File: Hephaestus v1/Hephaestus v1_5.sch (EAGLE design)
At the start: 31 parts, among them IC1 NC7SZ14P5X

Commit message: Schematic for Hephaestus V1_5 is essentially complete, need to select C2 and C1 values
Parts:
- removed PU_CL, PU_DA: 5k, resistor:R-US_R2512
- removed R_DEAD: (no value), resistor:R-US_R2512
- added ACS1: ACS712, heph_custom_comp:ACS712
- added C10: (no value), eagle-ltspice:CC0603
- added C11, C12: 4.7 uF, eagle-ltspice:CC0603
- added C13: 1 nF, eagle-ltspice:CC0603
- added C14: 0.1 uF, eagle-ltspice:CC0603
- added C15, C16, C9: 400 nF, eagle-ltspice:CC0603
- added D5: 12V, diode:DIODE-DO-214AC
- added D6, D7, D8, D9: 1N4148, diode:DIODE-DO35-10
- added IC2: NC7SZ14P5X, 74xx-little-de:NC7SZ14P5X
- added R10, R11, R12, R9: 1000, resistor:R-US_R2512
- added R13, R5: 5000, resistor:R-US_R2512
- added R6, R8: 55000, resistor:R-US_R2512
- added R7: (no value), resistor:R-US_R2512
- added U$23, U$24, U$25, U$26: STD15NF10, heph_custom_comp:STD15NF10
- added U$28: MCP3021, heph_custom_comp:MCP3021
- added U$6: A4957, heph_custom_comp:A4957
- C3: value (none) -> 400 nF
- D1, D2, D3, D4: value (none) -> 1N4148
- R1, R2, R3, R4: value (none) -> 1000
- renumbered CBYP to C8
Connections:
- removed net N$7 (its old number): U$1.RESET
- new net CA_B: C15.2, U$6.CA
- new net CB_B: C16.2, U$6.CB
- new net CUR_SENSE_B: ACS1.IP_N1, ACS1.IP_N2, D6.C, D8.C, U$23.D, U$24.D
- new net GHA_B: R10.2, R2.2, U$24.G
- new net GHB_B: R12.2, U$23.G
- new net GLA_B: R9.2, U$25.G
- new net GLB_B: R11.2, U$26.G
- new net MCU_GPIO_B_INV: IC2G$1.O, U$6.ALO
- new net MCU_SPD_B: U$6.BHI
- new net MOTOR_B+: C15.1, D6.A, D7.C, U$24.S, U$25.D, U$6.SA
- new net MOTOR_B-: C16.1, D8.A, D9.C, U$23.S, U$26.D, U$6.SB
- new net N$23: ACS1.VIOUT, U$28.AIN
- new net N$24: ACS1.FILTER, C13.2
- new net N$25: IC2G$1.I
- new net N$26: R9.1, U$6.GLA
- new net N$27: R11.1, U$6.GLB
- new net N$28: R12.1, U$6.GHB
- new net N$29: C10.2, U$6.VREG
- new net N$30: C4.2, U$6.CP2
- new net N$31: C4.1, U$6.CP1
- new net N$6: D5.A, R7.1, SIHFR9010.G
- new net RDEAD: R5.2, U$1.RESET
- new net RDEAD1: R13.2, U$6.RESET
- net CA_S: now also C9.2, U$1.CA; no longer C3.1, U$1.SA
- net CB_S: now also C3.2, U$1.CB; no longer C4.1, U$1.SB
- net GHA_S: no longer R2.2
- net GND: now also ACS1.GND, C10.1, C11.1, C12.1, C13.1, C14.1, D7.A, D9.A, R13.1, R5.1, R6.1, R7.2, R8.1, SV1.4, U$25.S, U$26.S, U$28.GND, U$6.AGND, U$6.GND_1, U$6.GND_2, U$6.GND_3; no longer R_DEAD.1, SIHFR9010.G, SV1.7
- net I2C_SCL_S: now also SV1.6, U$28.SCL; no longer PU_CL.2, SV1.5
- net I2C_SDA_S: now also SV1.5, U$28.SDA; no longer PU_DA.2, SV1.6
- net MCU_DIR_B: now also U$6.BLO
- net MCU_DIR_S: now also SV1.7; no longer SV1.4
- net MCU_FAULT_B: now also U$6.FAULT
- net MCU_FAULT_S: now also SV1.10; no longer SV1.1
- net MCU_GPIO_B: now also U$6.AHI
- net MCU_GPIO_S: now also SV1.9; no longer SV1.2
- net MCU_PWM_S: now also SV1.8; no longer SV1.3
- net MOTOR_S+: now also C9.1, U$1.SA
- net MOTOR_S-: now also C3.1, U$1.SB
- net N$12: now also R8.2, U$6.TDEAD; no longer C3.2, U$1.CA
- net N$14: now also R10.1, U$6.GHA; no longer C4.2, U$1.CB
- net N$8: now also R6.2; no longer R_DEAD.2
- net PP12V_2: now also ACS1.IP_P1, ACS1.IP_P2, C11.2, D5.C, SV3.1, U$6.VBB; no longer SV3.3
- net PP3V3: now also SV1.3; no longer SV1.8
- net PP5V: now also ACS1.VCC, C12.2, C14.2, SV1.1, SV1.2, U$28.VCC, U$6.VDD; no longer PU_CL.1, PU_DA.1, SV1.10, SV1.9
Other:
- note added: "Braking Current Sensing"
- note added: "Braking H-Bridge"
- note added: "SMAZ12"
- moved on the sheet: C1, C2, C3, C4, D1, D2, D3, D4, IC1, R1, R2, R3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

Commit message: Small changes and updates to the catch-diodes and P/N
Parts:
- removed C10, C4: (no value), eagle-ltspice:CC0603
- removed C11, C12: 4.7 uF, eagle-ltspice:CC0603
- removed C15, C16: 400 nF, eagle-ltspice:CC0603
- removed D6, D7, D8, D9: 1N4148, diode:DIODE-DO35-10
- removed IC2: NC7SZ14P5X, 74xx-little-de:NC7SZ14P5X
- removed R12: 1000, resistor:R-US_R2512
- removed R13: 5000, resistor:R-US_R2512
- removed U$18, U$28: MCP3021, heph_custom_comp:MCP3021
- removed U$23, U$24, U$25, U$26: STD15NF10, heph_custom_comp:STD15NF10
- added IC3: NC7SZ14P5X, 74xx-little-de:NC7SZ14P5X
- added U$22: MCP6L01, heph_custom_comp:MCP6L01
- added U$35: MCP3246, heph_custom_comp:MCP3246
- C1: value (none) -> 470 nF
- C2: value (none) -> 20 uF
- C3, C9: value 400 nF -> 1 uF
- D1, D2, D3, D4: value 1N4148 -> PMEG6020ETR; device diode:DIODE-DO35-10 -> heph_custom_comp:PMEG6020ETR
- R1, R2, R3, R4: value 1000 -> 100
- R10, R11, R9: value 1000 -> 5k
- R5: value 5000 -> 33k
- R6, R8: value 55000 -> 5k
- R7: value (none) -> 10000
- SIHFR9010: value FDD4141TO252 -> ATP302; device transistor-fet:FDD4141TO252 -> heph_custom_comp:ATP302
- U$10, U$5, U$8, U$9: value STD15NF10 -> FDMS037N08B; device heph_custom_comp:STD15NF10 -> heph_custom_comp:FDMS037N08B
- U$6: value A4957 -> MCP6L01; device heph_custom_comp:A4957 -> heph_custom_comp:MCP6L01
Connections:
- net MCU_GPIO_S_INV renamed MCU_DIR_S_INV
- net N$6 renamed RVP_G
- removed net CA_B: C15.2, U$6.CA
- removed net CB_B: C16.2, U$6.CB
- removed net GHB_B: R12.2, U$23.G
- removed net GLA_B: R9.2, U$25.G
- removed net GLB_B: R11.2, U$26.G
- removed net I2C_SCL_S: SV1.6, U$18.SCL, U$28.SCL
- removed net I2C_SDA_S: SV1.5, U$18.SDA, U$28.SDA
- removed net MCU_GPIO_B_INV: IC2G$1.O, U$6.ALO
- removed net MCU_SPD_B: U$6.BHI
- removed net MCU_SPD_S: U$1.BHI
- removed net MOTOR_B+: C15.1, D6.A, D7.C, U$24.S, U$25.D, U$6.SA
- removed net MOTOR_B-: C16.1, D8.A, D9.C, U$23.S, U$26.D, U$6.SB
- removed net N$12: R8.2, U$6.TDEAD
- removed net N$14: R10.1, U$6.GHA
- removed net N$21: ACS712.VIOUT, U$18.AIN
- removed net N$23: ACS1.VIOUT, U$28.AIN
- removed net N$25: IC2G$1.I
- removed net N$26: R9.1, U$6.GLA
- removed net N$27: R11.1, U$6.GLB
- removed net N$28: R12.1, U$6.GHB
- removed net N$29: C10.2, U$6.VREG
- removed net N$30: C4.2, U$6.CP2
- removed net N$31: C4.1, U$6.CP1
- removed net N$5: IC1G$1.I
- removed net RDEAD: R5.2, U$1.RESET
- removed net RDEAD1: R13.2, U$6.RESET
- new net CS_1: ACS712.VIOUT, U$35.CH1+
- new net CS_2: ACS1.VIOUT, U$35.CH2+
- new net I2C_SCL: SV1.6, U$35.SCL
- new net I2C_SDA: SV1.5, U$35.SDA
- new net MCU_PWM_S_INV: IC3G$1.O, U$1.BHI
- new net N$32: R5.1, U$1.RESET
- net CUR_SENSE_B: no longer D6.C, D8.C, U$23.D, U$24.D
- net GHA_B: no longer R10.2, U$24.G
- net GND: now also IC1P.GND, IC3P.GND, U$35.CH1-, U$35.CH2-, U$35.VSS; no longer C10.1, C11.1, C12.1, D7.A, D9.A, R13.1, R5.1, R8.1, U$18.GND, U$25.S, U$26.S, U$28.GND, U$6.AGND, U$6.GND_1, U$6.GND_2, U$6.GND_3
- net MCU_DIR_B: now also SV2.4; no longer SV2.1, U$6.BLO
- net MCU_DIR_S: now also IC1G$1.I
- net MCU_FAULT_B: now also SV2.1; no longer SV2.4, U$6.FAULT
- net MCU_GPIO_B: now also SV2.2; no longer SV2.3, U$6.AHI
- net MCU_GPIO_S: no longer U$1.AHI
- net MCU_PWM_B: now also SV2.3; no longer SV2.2
- net MCU_PWM_S: now also IC3G$1.I, U$1.AHI
- net PP12V_2: no longer C11.2, U$6.VBB
- net PP5V: now also IC1P.VCC, IC3P.VCC, R5.2, U$35.VDD; no longer C12.2, U$18.VCC, U$28.VCC, U$6.VDD
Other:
- note added: "Board to Steering Motor Conn"
- note added: "Boards to Brakes Motor Conn"
- note added: "Braking Current Sensor"
- note added: "Steering / Braking ADC"
- note added: "Steering Curent Sensor"
- note added: "UPDATE BRAKING H-BRIDGE"
- note added: "for r6 between 3, 240 kOhms, tdead ~ 50 + 7200 / (1.2 + (200 / rdead))"
- note removed: "Board to Steering Motor"
- note removed: "Boards to Brakes Motor"
- note removed: "Braking Current Sensing"
- note removed: "Steering Current Sensing"
- moved on the sheet: C13, C14, C7, C8, IC1, R10, R11, R5, R8, R9, SV2

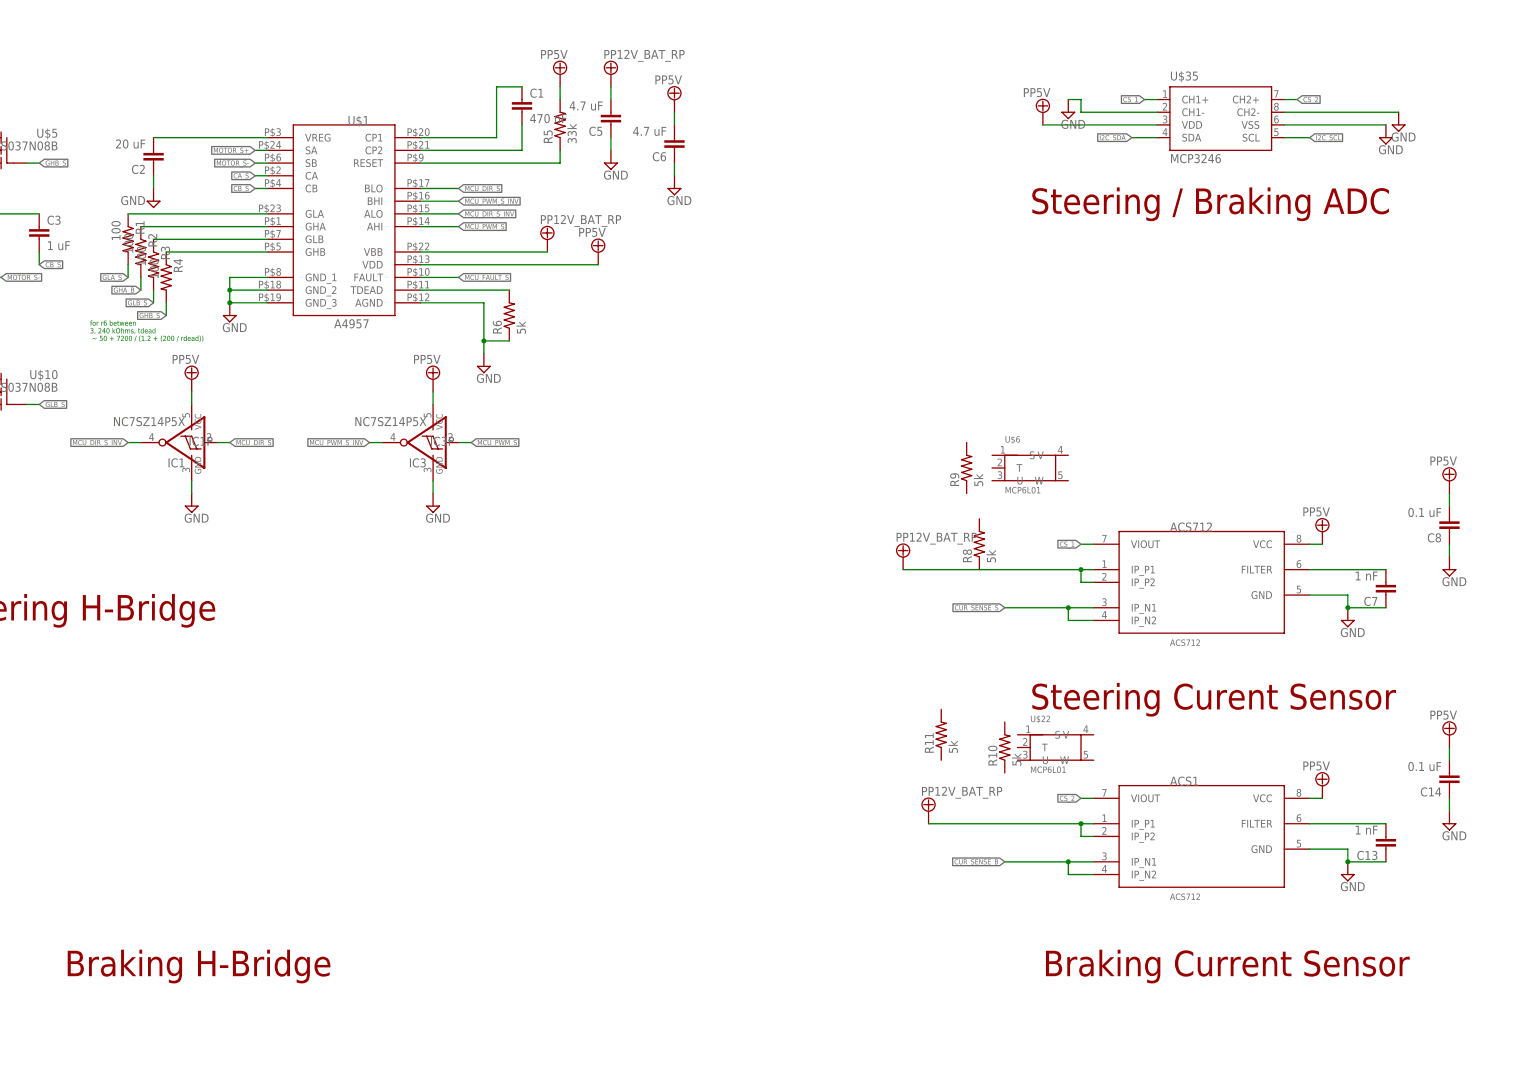
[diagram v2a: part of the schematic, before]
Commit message: Updated NMOS/PMOS/Catch Diodes to properly specc, added voltage divider / buffer between current transducer and ADC.
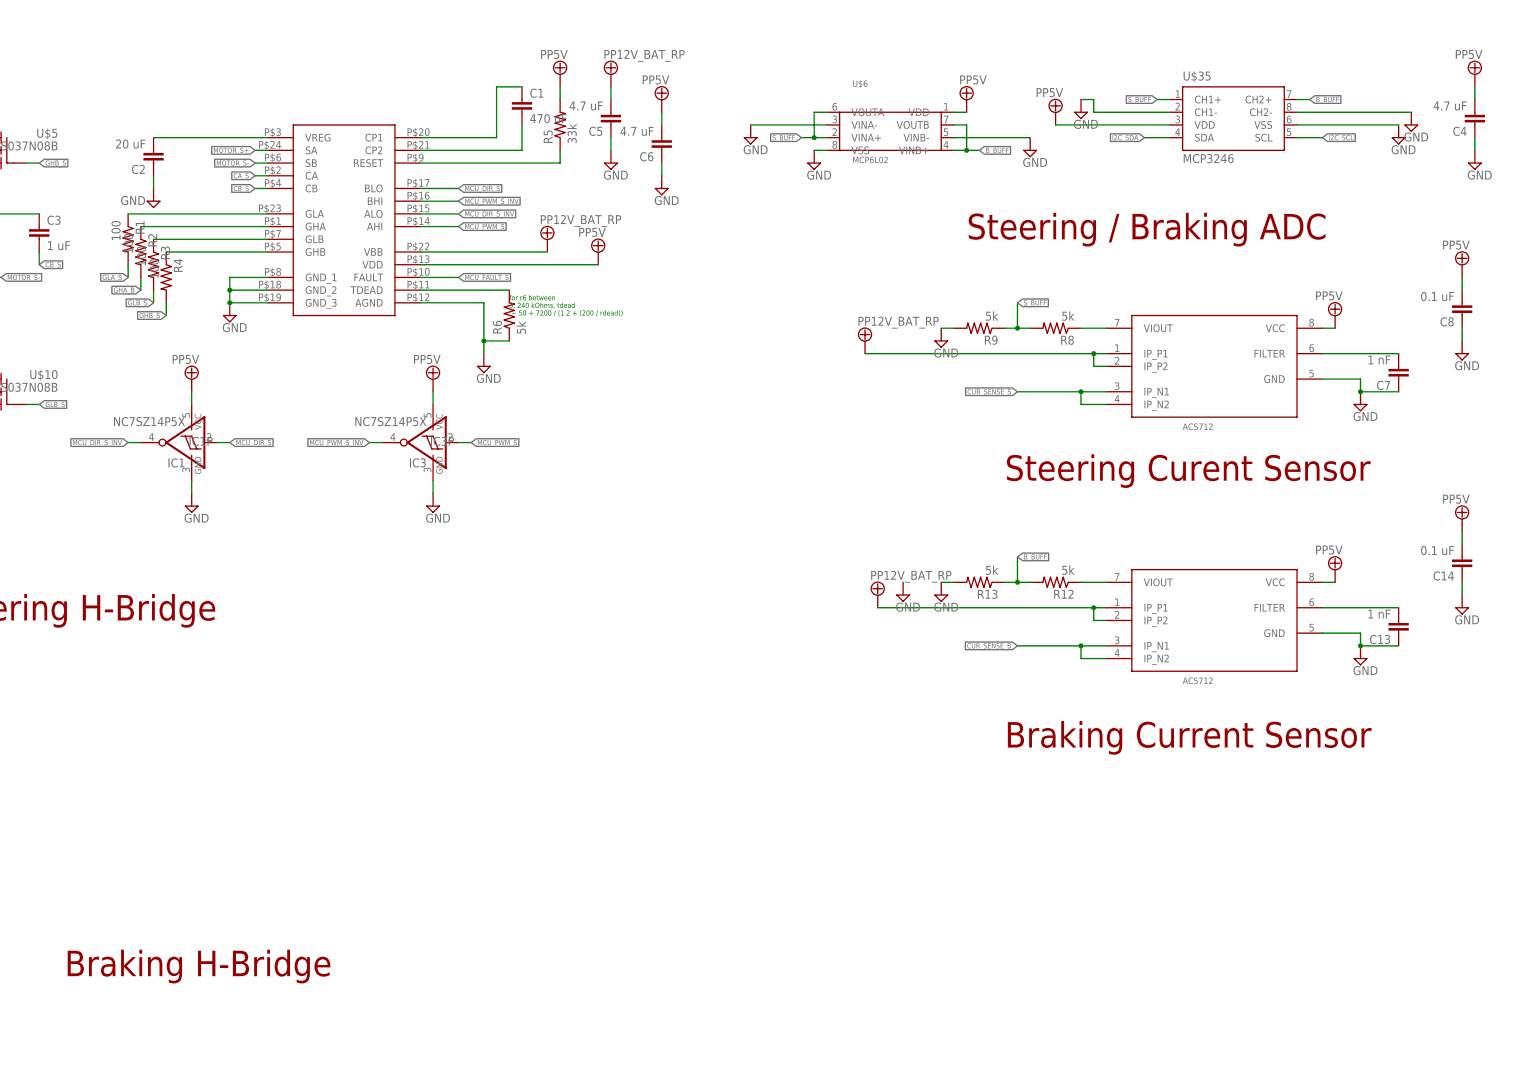
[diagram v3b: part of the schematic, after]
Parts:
- removed R10, R11: 5k, resistor:R-US_R2512
- removed U$22: MCP6L01, heph_custom_comp:MCP6L01
- added C4: 4.7 uF, eagle-ltspice:CC0603
- added R12, R13: 5k, resistor:R-US_R2512
- U$6: value MCP6L01 -> MCP6L02; device heph_custom_comp:MCP6L01 -> heph_custom_comp:MCP6L02
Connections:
- new net B_BUFF: R12.2, R13.1, U$35.CH2+, U$6.VINB+, U$6.VOUTB
- new net S_BUFF: R8.2, R9.1, U$35.CH1+, U$6.VINA+, U$6.VOUTA
- net CS_1: now also R8.1; no longer U$35.CH1+
- net CS_2: now also R12.1; no longer U$35.CH2+
- net GND: now also C4.1, R13.2, R9.2, U$6.VINA-, U$6.VINB-, U$6.VSS
- net PP5V: now also C4.2, U$6.VDD
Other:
- moved on the sheet: C13, C14, C6, C7, C8, R8, R9, U$35

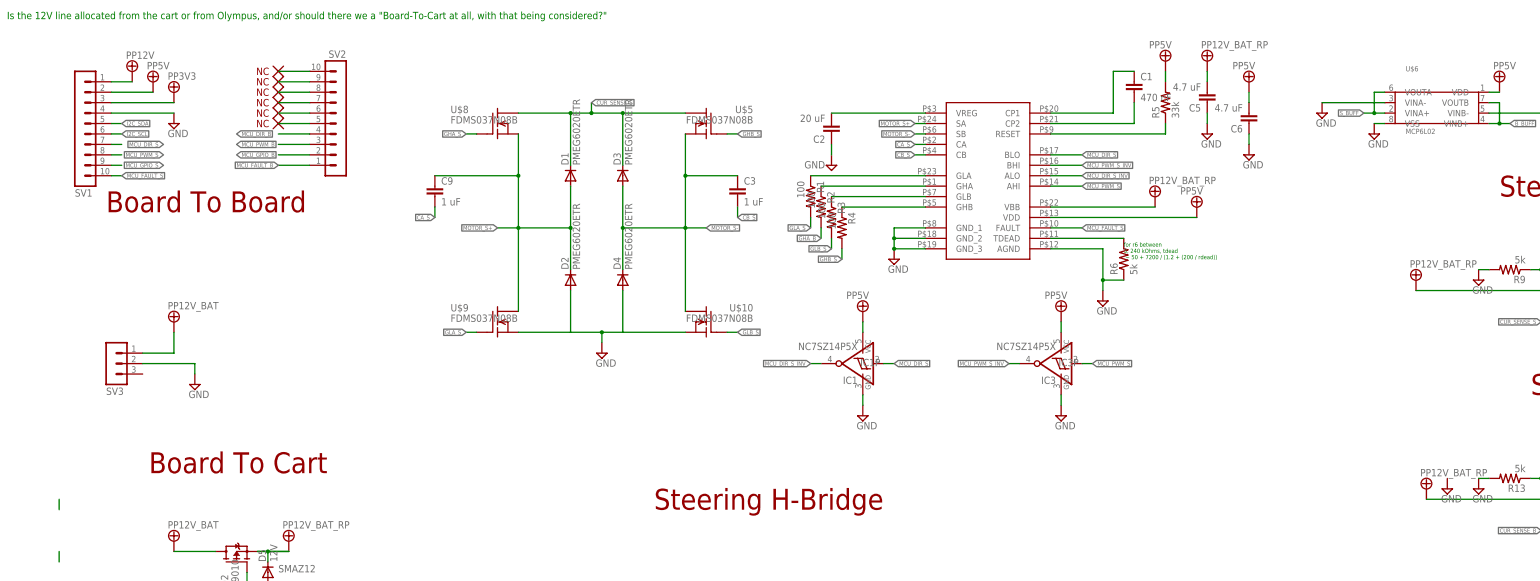
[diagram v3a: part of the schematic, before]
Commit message: Most recent revision; added voltage divider / buffer to make current transducers compatible with ADC input voltage.
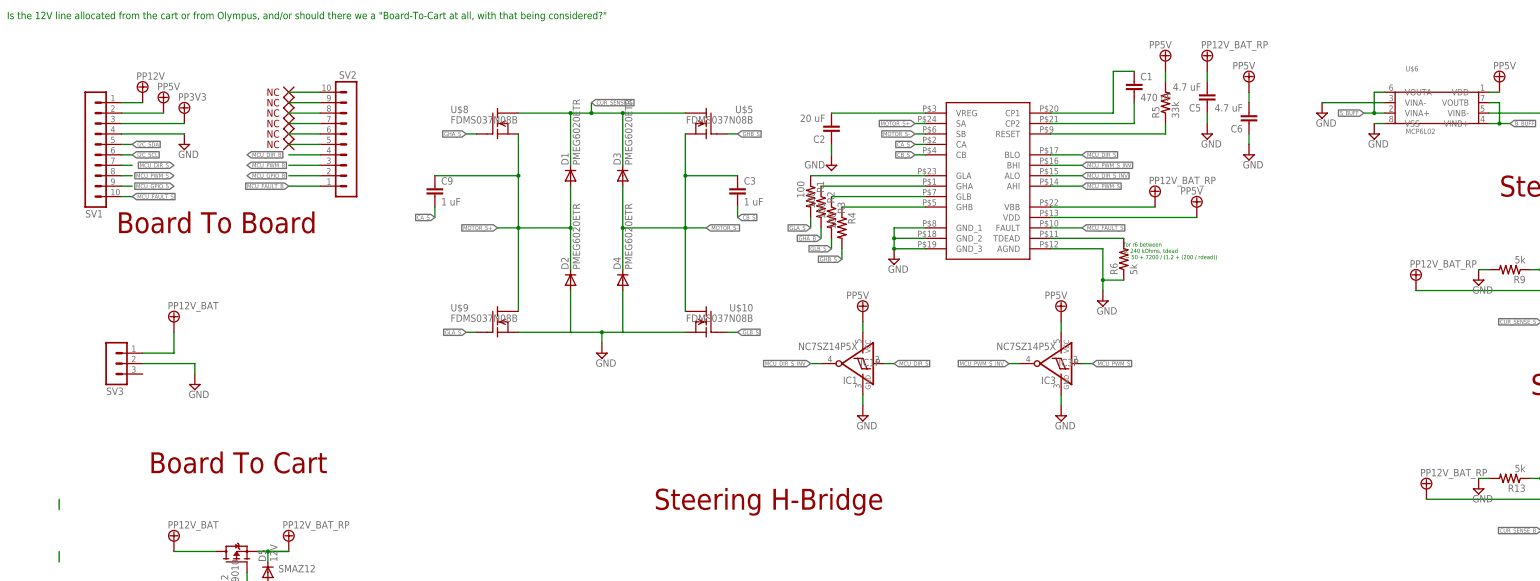
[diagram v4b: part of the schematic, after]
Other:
- moved on the sheet: SV1, SV2

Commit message: Fixed layouts and pin ordering / connections.
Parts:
- C2: value 20 uF -> 22 uF
- R7: value 10000 -> 10k
- U$1: DIGI (none) -> 620-1491-1-ND
- U$35: DIG (none) -> MCP3426A0-E/SN-ND
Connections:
- new net B_SENSE: U$6.VINB-, U$6.VOUTB
- new net S_SENSE: U$6.VINA-, U$6.VOUTA
- net B_BUFF: no longer U$6.VOUTB
- net GND: no longer U$6.VINA-, U$6.VINB-
- net S_BUFF: no longer U$6.VOUTA
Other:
- moved on the sheet: R1, R3, R4
